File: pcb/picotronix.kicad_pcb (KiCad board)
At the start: 2 copper layers, 88.5 x 67 mm, 25 parts, among them J1 Conn_02x04_Odd_Even, J2 Conn_02x04_Odd_Even, J3 DEBUG, J4 DB25_Male, U1 Pico, U2 TXS0104PW, U3 DAC7562SDGST, U4 TL074

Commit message: update pcb
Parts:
- removed C3, C4: C, Capacitor_SMD:C_0603_1608Metric_Pad1.08x0.95mm_HandSolder
- removed JP1: filter_bypass, Jumper:SolderJumper-2_P1.3mm_Open_Pad1.0x1.5mm
- removed R3: R_US, Resistor_SMD:R_0603_1608Metric_Pad0.98x0.95mm_HandSolder
- added RN1: 10k, Resistor_SMD:R_Array_Convex_4x1206, F.Cu at (101.2, 122.2)
- added RN2: 470, Resistor_SMD:R_Array_Convex_4x1206, F.Cu at (133.2, 109.5)
- added RN3: 4.99k, Resistor_SMD:R_Array_Convex_4x1206, F.Cu at (108.2, 122.2)
- added TP1: Z Test, TestPoint:TestPoint_Pad_2.0x2.0mm, F.Cu at (132.5, 101.8)
- added TP2: Y Test, TestPoint:TestPoint_Pad_2.0x2.0mm, F.Cu at (119.5, 125.8)
- added TP3: X test, TestPoint:TestPoint_Pad_2.0x2.0mm, F.Cu at (125.0, 125.8)
- J4: footprint Connector_Dsub:DSUB-25_Male_Horizontal_P2.77x2.54mm_EdgePinOffset9.40mm -> Connector_Dsub:DSUB-25_Male_Horizontal_P2.77x2.84mm_EdgePinOffset9.90mm_Housed_MountingHolesOffset11.32mm
- R2: value R_US -> 10k
- RV1: value Z Trim -> 20k
- RV2: value X Trim -> 20k
- RV3: value Y Trim -> 20k
- U2: value TXS0104PW -> LSF0204DPWR
- U3: value DAC7562SDGST -> AD5663R; footprint Package_SO:VSSOP-10_3x3mm_P0.5mm -> Package_SO:MSOP-10_3x3mm_P0.5mm
- U4: value TL074 -> ADA4891-3; footprint Package_SO:SOIC-14_3.9x8.7mm_P1.27mm -> Package_SO:TSSOP-14_4.4x5mm_P0.65mm
- moved R2 18.1 mm to (108.2, 116.2), turned to -90 degrees
- moved H2 15.0 mm to (131.0, 69.5)
- moved H4 15.0 mm to (131.0, 126.5)
- moved RV1 8.40 mm to (116.5, 109.0)
- moved RV3 8.40 mm to (116.5, 117.2)
- moved C5 5.62 mm to (124.2, 104.0)
- moved U4 5.27 mm to (124.2, 109.0)
- moved C6 5.26 mm to (124.2, 101.2)
- moved RV2 3.26 mm to (116.5, 102.2)
- moved J4 0.75 mm to (138.2, 114.6)
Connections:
- R2 pad 1: Net-(JP1-Pad1) -> GND
- RV1 pad 1: /z_pwm -> Net-(RV1-Pad1)
- RV1 pad 2: Net-(JP1-Pad1) -> Net-(RV1-Pad2)
- RV3 pad 1: Net-(RV3-Pad1) -> Net-(RN1-Pad4)
- U1 pad 19: unconnected-(U1-Pad19) -> /z_{1}
- U1 pad 20: unconnected-(U1-Pad20) -> /z_{2}
- U1 pad 21: /z_pwm -> /z_{3}
- U1 pad 22: /~{CS} -> /z_{4}
- U1 pad 27: /erase_l -> /~{CS}
- U1 pad 29: /non_store_l -> /erase_l
- U1 pad 31: /erase_interval_l -> /non_store_l
- U1 pad 32: /var_bright_l -> /erase_interval_l
- U1 pad 34: unconnected-(U1-Pad34) -> /var_bright_l
- U3 pad 1: Net-(RV2-Pad1) -> Net-(RV1-Pad1)
- U3 pad 2: Net-(RV3-Pad1) -> Net-(RV2-Pad1)
- U4 pad 1: /Y_OUTPUT -> unconnected-(U4-Pad1)
- U4 pad 10: Net-(C3-Pad2) -> Net-(RV3-Pad2)
- U4 pad 12: unconnected-(U4-Pad12) -> Net-(RV2-Pad2)
- U4 pad 13: unconnected-(U4-Pad13) -> Net-(RN2-Pad8)
- U4 pad 14: unconnected-(U4-Pad14) -> (no net)
- U4 pad 2: /Y_OUTPUT -> unconnected-(U4-Pad2)
- U4 pad 3: Net-(RV2-Pad2) -> unconnected-(U4-Pad3)
- U4 pad 5: Net-(RV3-Pad2) -> Net-(RV1-Pad2)
- U4 pad 6: /X_OUTPUT -> Net-(RN2-Pad7)
- U4 pad 7: /X_OUTPUT -> Net-(RN2-Pad7)
- U4 pad 8: /Z_OUTPUT -> Net-(RN2-Pad6)
- U4 pad 9: /Z_OUTPUT -> Net-(RN2-Pad6)
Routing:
- net /z_{2}: track 0.00 -> 25.2 mm, vias 0 -> 2
- net /z_{1}: track 0.00 -> 22.1 mm
- net /z_pwm: track 17.5 -> 0.00 mm
- net /Y_OUTPUT: track 17.4 -> 33.3 mm, vias 1 -> 0
- net Net-(RN1-Pad4): track 0.00 -> 15.6 mm, vias 0 -> 2
- net Net-(C3-Pad2): track 15.6 -> 0.00 mm
- net Net-(RN1-Pad3): track 0.00 -> 12.7 mm
- net /z_{4}: track 0.00 -> 12.5 mm
- net Net-(RN2-Pad7): track 0.00 -> 12.4 mm
- net /X_OUTPUT: track 13.9 -> 26.0 mm, vias 1 -> 0
- net Net-(R2-Pad2): track 5.78 -> 17.5 mm
- net /~{CS}: track 9.76 -> 21.4 mm
- net Net-(JP1-Pad1): track 9.68 -> 0.00 mm
- net Net-(RV3-Pad1): track 9.03 -> 0.00 mm
- net Net-(RV3-Pad2): track 5.94 -> 14.8 mm, vias 0 -> 2
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
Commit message: pcb rev2 routed
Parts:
- added C10: 0.1u, Capacitor_SMD:C_0603_1608Metric_Pad1.08x0.95mm_HandSolder, F.Cu at (109.0, 77.5)
- added C11: 0.1u, Capacitor_SMD:C_0603_1608Metric_Pad1.08x0.95mm_HandSolder, F.Cu at (147.2, 109.8)
- added C3: 0.1u, Capacitor_SMD:C_0603_1608Metric_Pad1.08x0.95mm_HandSolder, F.Cu at (159.2, 81.0)
- added C4: 0.1u, Capacitor_SMD:C_0603_1608Metric_Pad1.08x0.95mm_HandSolder, F.Cu at (165.0, 81.0)
- added C7: 1u, Capacitor_SMD:C_0603_1608Metric_Pad1.08x0.95mm_HandSolder, F.Cu at (103.5, 72.2)
- added C8: 1u, Capacitor_SMD:C_0603_1608Metric_Pad1.08x0.95mm_HandSolder, F.Cu at (103.6, 69.5)
- added C9: 0.1u, Capacitor_SMD:C_0603_1608Metric_Pad1.08x0.95mm_HandSolder, F.Cu at (109.0, 80.2)
- added JP1: FMT_SET, Jumper:SolderJumper-2_P1.3mm_Open_TrianglePad1.0x1.5mm, F.Cu at (123.5, 74.8)
- added JP2: MD1_SET, Jumper:SolderJumper-2_P1.3mm_Open_TrianglePad1.0x1.5mm, F.Cu at (123.5, 78.5)
- added JP3: MD0_SET, Jumper:SolderJumper-2_P1.3mm_Open_TrianglePad1.0x1.5mm, F.Cu at (123.5, 82.2)
- added R3: 10k, Resistor_SMD:R_0603_1608Metric_Pad0.98x0.95mm_HandSolder, F.Cu at (150.0, 130.4)
- added SW1: BTN0, Button_Switch_SMD:SW_SPST_TL3305A, F.Cu at (99.5, 121.5)
- added SW2: BTN1, Button_Switch_SMD:SW_SPST_TL3305A, F.Cu at (99.5, 128.5)
- added SW3: RESET, Button_Switch_SMD:SW_SPST_TL3305A, F.Cu at (132.5, 80.8)
- added U5: W25Q128JVS, Package_SO:SOIC-8_5.23x5.23mm_P1.27mm, F.Cu at (123.0, 129.0)
- added U6: PCM1808, Package_SO:TSSOP-14_4.4x5mm_P0.65mm, F.Cu at (116.8, 78.5)
- J1: value Conn_02x04_Odd_Even -> AudioJack3_Ground; footprint Connector_PinSocket_2.54mm:PinSocket_2x04_P2.54mm_Vertical -> Connector_Audio:Jack_3.5mm_CUI_SJ-3524-SMT_Horizontal
- J2: value Conn_02x04_Odd_Even -> ESP-01 Connector
- J3: footprint Connector_PinHeader_2.54mm:PinHeader_1x03_P2.54mm_Vertical -> Connector_PinHeader_2.54mm:PinHeader_2x03_P2.54mm_Vertical
- RN2: value 470 -> 4.99k
- RN3: value 4.99k -> 470
- moved R2 60.9 mm to (163.2, 90.0), turned to 180 degrees
- moved RN3 58.9 mm to (166.8, 115.0), turned to 180 degrees
- moved J3 57.0 mm to (142.7, 94.0), turned to 0 degrees
- moved J2 49.9 mm to (112.8, 124.0)
- moved U2 49.0 mm to (162.0, 86.2)
- moved H4 48.5 mm to (178.8, 135.0)
- moved H2 48.0 mm to (179.0, 70.0)
- moved RN1 46.6 mm to (147.8, 124.7), turned to 180 degrees
- moved TP2 46.0 mm to (165.5, 127.0), turned to -90 degrees
- moved RV1 45.0 mm to (159.5, 122.2), turned to 90 degrees
- moved C1 44.6 mm to (126.8, 123.9)
- moved TP3 40.8 mm to (165.5, 131.0), turned to -90 degrees
- moved RV2 40.4 mm to (154.2, 116.8)
- moved TP1 39.2 mm to (165.5, 123.0), turned to -90 degrees
- moved RV3 38.3 mm to (154.2, 110.8)
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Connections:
- C2 pad 1: +5V -> Net-(C2-Pad1)
- J2 pad 2: /gpio6 -> /UART0_RX
- J2 pad 3: /gpio7 -> unconnected-(J2-Pad3)
- J2 pad 4: /gpio8 -> /esp_en
- J2 pad 5: /gpio9 -> unconnected-(J2-Pad5)
- J2 pad 6: /gpio10 -> unconnected-(J2-Pad6)
- J2 pad 7: /gpio11 -> /UART0_TX
- J3 pad 2: Net-(J3-Pad2) -> /dbg_rx
- J3 pad 3: GND -> Net-(J3-Pad3)
- R1 pad 1: Net-(R1-Pad1) -> +3V3
- R1 pad 2: +3V3 -> /esp_en
- R2 pad 1: GND -> Net-(R2-Pad1)
- R2 pad 2: Net-(R2-Pad2) -> +3V3
- RN1 pad 1: Net-(R2-Pad2) -> Net-(R3-Pad2)
- RN2 pad 1: /X_OUTPUT -> Net-(RN1-Pad2)
- RN2 pad 2: /Y_OUTPUT -> Net-(RN1-Pad3)
- RN2 pad 3: /Z_OUTPUT -> Net-(RN1-Pad4)
- RN2 pad 6: Net-(RN2-Pad6) -> Net-(RN1-Pad3)
- RN2 pad 7: Net-(RN2-Pad7) -> Net-(RN1-Pad2)
- RN2 pad 8: Net-(RN2-Pad8) -> Net-(R3-Pad2)
- RN3 pad 1: Net-(RN1-Pad2) -> /X_OUTPUT
- RN3 pad 2: Net-(RN1-Pad2) -> /Y_OUTPUT
- RN3 pad 3: Net-(RN1-Pad4) -> /Z_OUTPUT
- RN3 pad 6: Net-(RN1-Pad3) -> Net-(RN3-Pad6)
- RN3 pad 7: Net-(RN1-Pad3) -> Net-(RN3-Pad7)
- RN3 pad 8: Net-(R2-Pad2) -> Net-(RN3-Pad8)
- RV1 pad 1: Net-(RV1-Pad1) -> Net-(RN1-Pad4)
- RV3 pad 1: Net-(RN1-Pad4) -> Net-(RV3-Pad1)
- U1 pad 1: /gpio0 -> /UART0_TX
- U1 pad 10: /gpio7 -> /erase_l
- U1 pad 11: /gpio8 -> /FLASH_MISO
- U1 pad 12: /gpio9 -> /FLASH_CS
- U1 pad 14: /gpio10 -> /FLASH_SCK
- U1 pad 15: /gpio11 -> /FLASH_MOSI
- U1 pad 16: unconnected-(U1-Pad16) -> /z_{1}
- U1 pad 17: unconnected-(U1-Pad17) -> /z_{2}
- U1 pad 19: /z_{1} -> /z_{3}
- U1 pad 2: /gpio1 -> /UART0_RX
- U1 pad 20: /z_{2} -> /z_{4}
- U1 pad 21: /z_{3} -> /XY_FLUSH
- U1 pad 22: /z_{4} -> /~{CS}
- U1 pad 26: /XY_FLUSH -> /non_store_l
- U1 pad 27: /~{CS} -> /i2s_mclk
- U1 pad 29: /erase_l -> /i2s_bck
- U1 pad 30: unconnected-(U1-Pad30) -> Net-(SW3-Pad1)
- U1 pad 31: /non_store_l -> /i2s_dout
- U1 pad 32: /erase_interval_l -> /i2s_lrclk
- U1 pad 4: /gpio2 -> Net-(SW1-Pad2)
- U1 pad 41: Net-(J3-Pad2) -> Net-(J3-Pad3)
- U1 pad 5: /gpio3 -> Net-(SW2-Pad2)
- U1 pad 6: /gpio4 -> /dbg_tx
- U1 pad 7: /gpio5 -> /dbg_rx
- U1 pad 9: /gpio6 -> /erase_interval_l
- U2 pad 8: Net-(R1-Pad1) -> Net-(R2-Pad1)
- U3 pad 1: Net-(RV1-Pad1) -> Net-(RV2-Pad1)
- U3 pad 2: Net-(RV2-Pad1) -> Net-(RV3-Pad1)
- U4 pad 10: Net-(RV3-Pad2) -> Net-(RV1-Pad2)
- U4 pad 12: Net-(RV2-Pad2) -> Net-(RV3-Pad2)
- U4 pad 13: Net-(RN2-Pad8) -> Net-(RN3-Pad8)
- U4 pad 5: Net-(RV1-Pad2) -> Net-(RV2-Pad2)
- U4 pad 6: Net-(RN2-Pad7) -> Net-(RN3-Pad7)
- U4 pad 7: Net-(RN2-Pad7) -> Net-(RN3-Pad7)
- U4 pad 8: Net-(RN2-Pad6) -> Net-(RN3-Pad6)
- U4 pad 9: Net-(RN2-Pad6) -> Net-(RN3-Pad6)
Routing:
- net +3V3: track 113.5 -> 224.9 mm, vias 2 -> 6
- net +5V: track 65.6 -> 128.6 mm, vias 2 -> 3
- net /erase_interval_l: track 9.52 -> 66.9 mm, vias 0 -> 2
- net /dbg_tx: track 0.00 -> 53.2 mm, vias 0 -> 1
- net /UART0_RX: track 0.00 -> 52.8 mm
- net /dbg_rx: track 0.00 -> 51.9 mm, vias 0 -> 1
- net /var_bright_l: track 11.4 -> 62.5 mm, vias 0 -> 1
- net /erase_l: track 13.8 -> 63.4 mm, vias 0 -> 2
- net /UART0_TX: track 0.00 -> 47.4 mm
- net /non_store_l: track 9.76 -> 40.7 mm
- net /XY_FLUSH: track 11.3 -> 35.6 mm
- net /FLASH_MOSI: track 0.00 -> 23.7 mm
- net /FLASH_SCK: track 0.00 -> 23.1 mm
- net Net-(SW3-Pad1): track 0.00 -> 22.5 mm, vias 0 -> 1
- net Net-(C7-Pad1): track 0.00 -> 21.8 mm
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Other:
- board size 88.5 x 67 mm -> 97.8 x 75 mm
- board text added: "SWCLK"
- board text added: "SWDIO"
- board text added: "esp orientation"
- board text added: "gnd"
- board text added: "picotronix rev. 2 saji champlin 2022"
- board text added: "rx"
- board text added: "tx"
- board text added: "x"
- board text added: "y"
- board text added: "y-axis"
- board text added: "z"
- board text removed: "picotronix rev.1 saji champlin 03/2022"

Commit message: pcb final revision
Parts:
- removed the R2 at (163.2, 90.0)
- removed TP1: Z Test, TestPoint:TestPoint_Pad_2.0x2.0mm
- removed TP2: Y Test, TestPoint:TestPoint_Pad_2.0x2.0mm
- removed TP3: X test, TestPoint:TestPoint_Pad_2.0x2.0mm
- added R1: 10k, Resistor_SMD:R_0603_1608Metric_Pad0.98x0.95mm_HandSolder, F.Cu at (122.2, 124.4)
- added TP10: ESP_BOOT, TestPoint:TestPoint_Pad_D1.0mm, F.Cu at (115.7, 137.2)
- added TP11: ESP_GPIO16, TestPoint:TestPoint_Pad_D1.0mm, F.Cu at (111.8, 137.2)
- added TP20: Z Test, TestPoint:TestPoint_Pad_D1.0mm, F.Cu at (165.6, 123.0)
- added TP21: Y Test, TestPoint:TestPoint_Pad_D1.0mm, F.Cu at (165.6, 127.0)
- added TP22: X test, TestPoint:TestPoint_Pad_D1.0mm, F.Cu at (165.6, 131.0)
- added TP9: ESP_GPIO2, TestPoint:TestPoint_Pad_D1.0mm, F.Cu at (119.1, 137.2)
- moved J2 3.11 mm to (143.7, 91.0), turned to 90 degrees
- moved J1 2.30 mm to (92.2, 80.0)
- moved C2 0.25 mm to (103.8, 72.2)
- moved C1 0.11 mm to (103.8, 69.5)
- renumbered C8 to C1, C11 to C10, C1 to C11, C7 to C2, C2 to C3, C10 to C4, C9 to C5, C3 to C6, C4 to C7, C5 to C8, C6 to C9, J3 to J2, J4 to J3, J2 to J4, R1 to R2, RN3 to RN1, RN1 to RN2, RN2 to RN3, RV3 to RV1, RV1 to RV3, SW3 to SW1, SW1 to SW2, SW2 to SW3, U6 to U1, U1 to U3, U3 to U5, U5 to U6
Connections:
- J4 pad 3: unconnected-(J2-Pad3) -> /esp_gpio2
- J4 pad 5: unconnected-(J2-Pad5) -> /esp_boot
- J4 pad 6: unconnected-(J2-Pad6) -> /esp_gpio16
- RN1 pad 7: Net-(RN3-Pad7) -> Net-(RN1-Pad7)
- RN1 pad 8: Net-(RN3-Pad8) -> Net-(RN1-Pad8)
- RV1 pad 2: Net-(RV3-Pad2) (its old number) -> Net-(RV1-Pad2)
- U2 pad 8: Net-(R2-Pad1) -> +3V3
- U4 pad 12: Net-(RV3-Pad2) (its old number) -> Net-(RV2-Pad2)
- U4 pad 13: Net-(RN3-Pad8) -> Net-(RN1-Pad7)
- U4 pad 14: (no net) -> Net-(RN1-Pad7)
- U4 pad 5: Net-(RV2-Pad2) -> Net-(RV1-Pad2)
- U4 pad 6: Net-(RN3-Pad7) -> Net-(RN1-Pad8)
- U4 pad 7: Net-(RN3-Pad7) -> Net-(RN1-Pad8)
- U6 pad 3: unconnected-(U5-Pad3) -> Net-(R1-Pad2)
- U6 pad 7: unconnected-(U5-Pad7) -> Net-(R1-Pad2)
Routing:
- net Net-(RN1-Pad8): track 0.00 -> 16.3 mm, vias 0 -> 2
- net Net-(RN3-Pad8): track 15.3 -> 0.00 mm
- net Net-(RN1-Pad7): track 0.00 -> 14.6 mm
- net Net-(RN3-Pad7): track 14.2 -> 0.00 mm, vias 2 -> 0
- net /esp_gpio2: track 0.00 -> 13.3 mm
- net Net-(R1-Pad2): track 0.00 -> 12.1 mm
- net /esp_gpio16: track 0.00 -> 12.0 mm, vias 0 -> 1
- net Net-(RV3-Pad2) (its old number): track 11.9 -> 0.00 mm
- net /esp_boot: track 0.00 -> 10.5 mm
- net /dbg_tx: track 53.2 -> 62.8 mm
- net Net-(SW1-Pad1): track 22.5 -> 29.7 mm
- net Net-(SW2-Pad2): track 12.5 -> 19.7 mm
- net /dbg_rx: track 51.9 -> 58.8 mm
- net +3V3: track 224.9 -> 218.1 mm
- net Net-(SW3-Pad2): track 19.5 -> 25.9 mm, vias 0 -> 1
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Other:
- board text added: "FMT"
- board text added: "MD0"
- board text added: "MD1"
- board text added: "x-axis"
- board text added: "z-axis"

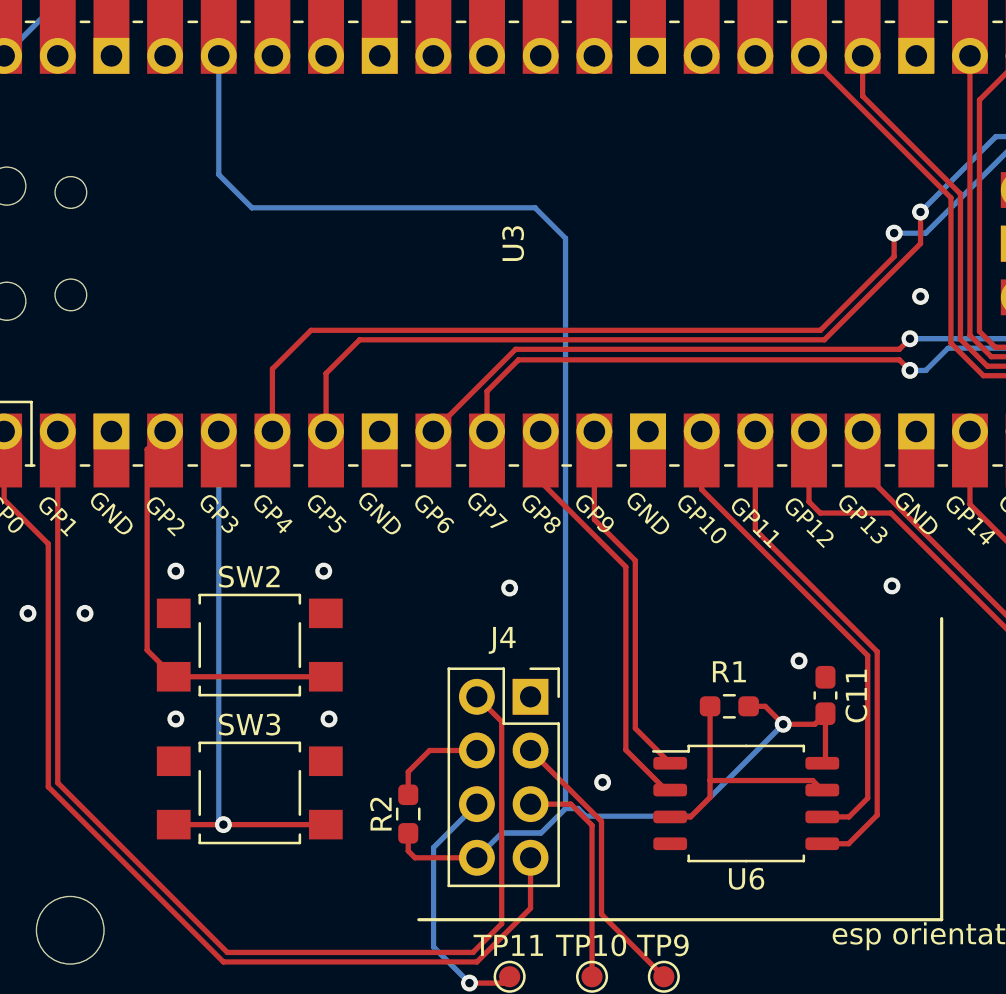
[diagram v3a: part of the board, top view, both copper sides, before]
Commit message: minor revisions to board and schematic (mostly cleanup)
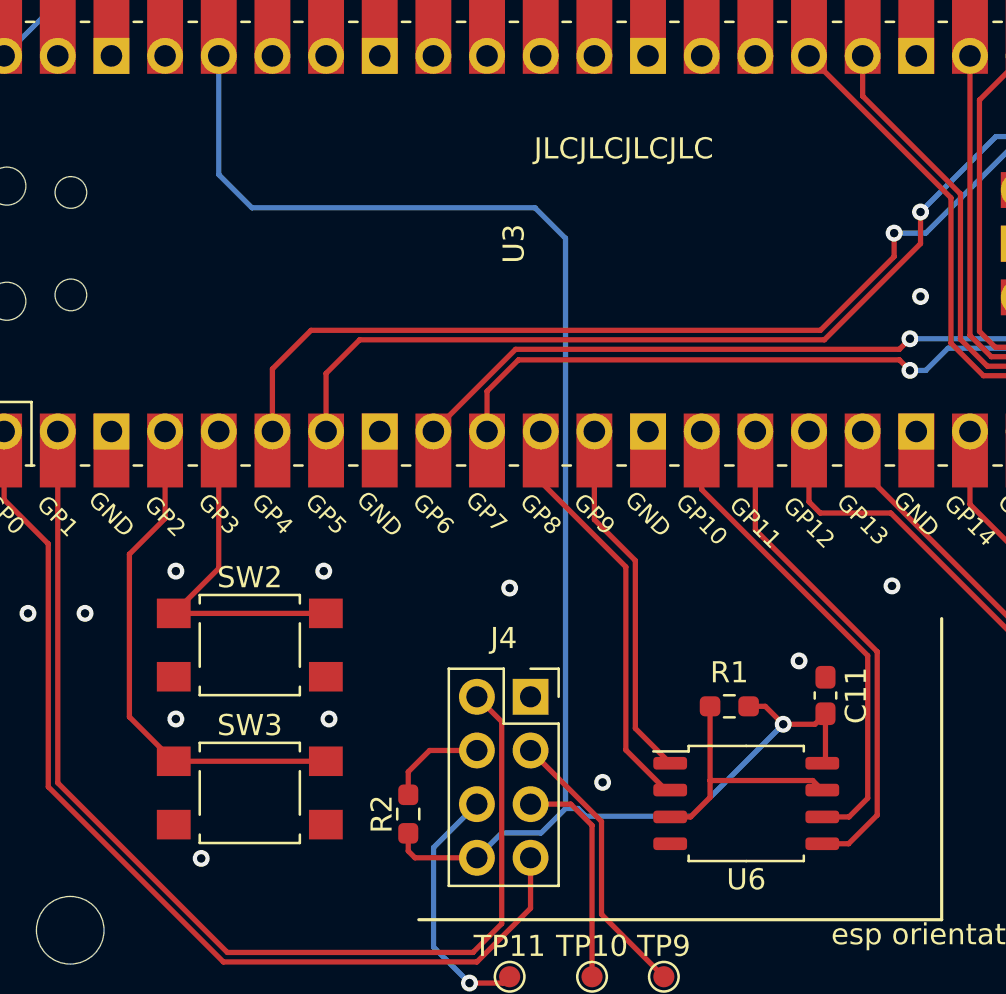
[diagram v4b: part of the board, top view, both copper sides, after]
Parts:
- turned C11 to -90 degrees
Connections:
- net /erase_interval_l renamed /e_interval_l
- C11 pad 1: +3V3 -> GND
- C11 pad 2: GND -> +3V3
- C6 pad 1: +3V3 -> GND
- C6 pad 2: GND -> +3V3
- SW2 pad 1: GND -> /btn0
- SW2 pad 2: Net-(SW2-Pad2) -> GND
- SW3 pad 1: GND -> /btn1
- SW3 pad 2: Net-(SW3-Pad2) -> GND
- U3 pad 4: Net-(SW2-Pad2) -> /btn1
- U3 pad 5: Net-(SW3-Pad2) -> /btn0
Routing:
- net Net-(SW3-Pad2): track 25.9 -> 0.00 mm, vias 1 -> 0
- net /btn1: track 0.00 -> 24.4 mm
- net Net-(SW2-Pad2): track 19.7 -> 0.00 mm
- net /btn0: track 0.00 -> 16.7 mm
- net GND: vias 46 -> 47
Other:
- board text added: "JLCJLCJLCJLC"

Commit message: some pcb tweaks (ordered this commit for rev 1)
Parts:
- turned C6 to -90 degrees
- renumbered TP20 to TP1, TP21 to TP2, TP22 to TP3, TP11 to TP4, TP10 to TP5, TP9 to TP6
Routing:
- net /~{CS}: track 28.6 -> 27.4 mm
- net +3V3: track 218.1 -> 219.2 mm, vias 6 -> 5
- net Net-(C2-Pad2): track 19.0 -> 18.3 mm
